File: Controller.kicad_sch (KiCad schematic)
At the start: 14 parts, among them SW1 PTS526 SK15 SMTR2 LFS, SW2 DS04-254-2-01BK-SMT, U1 STM32WB55RCVx, Y1 ECS-320-8-33-RWY-TR, Y2 ECS-.327-9-12R-TR

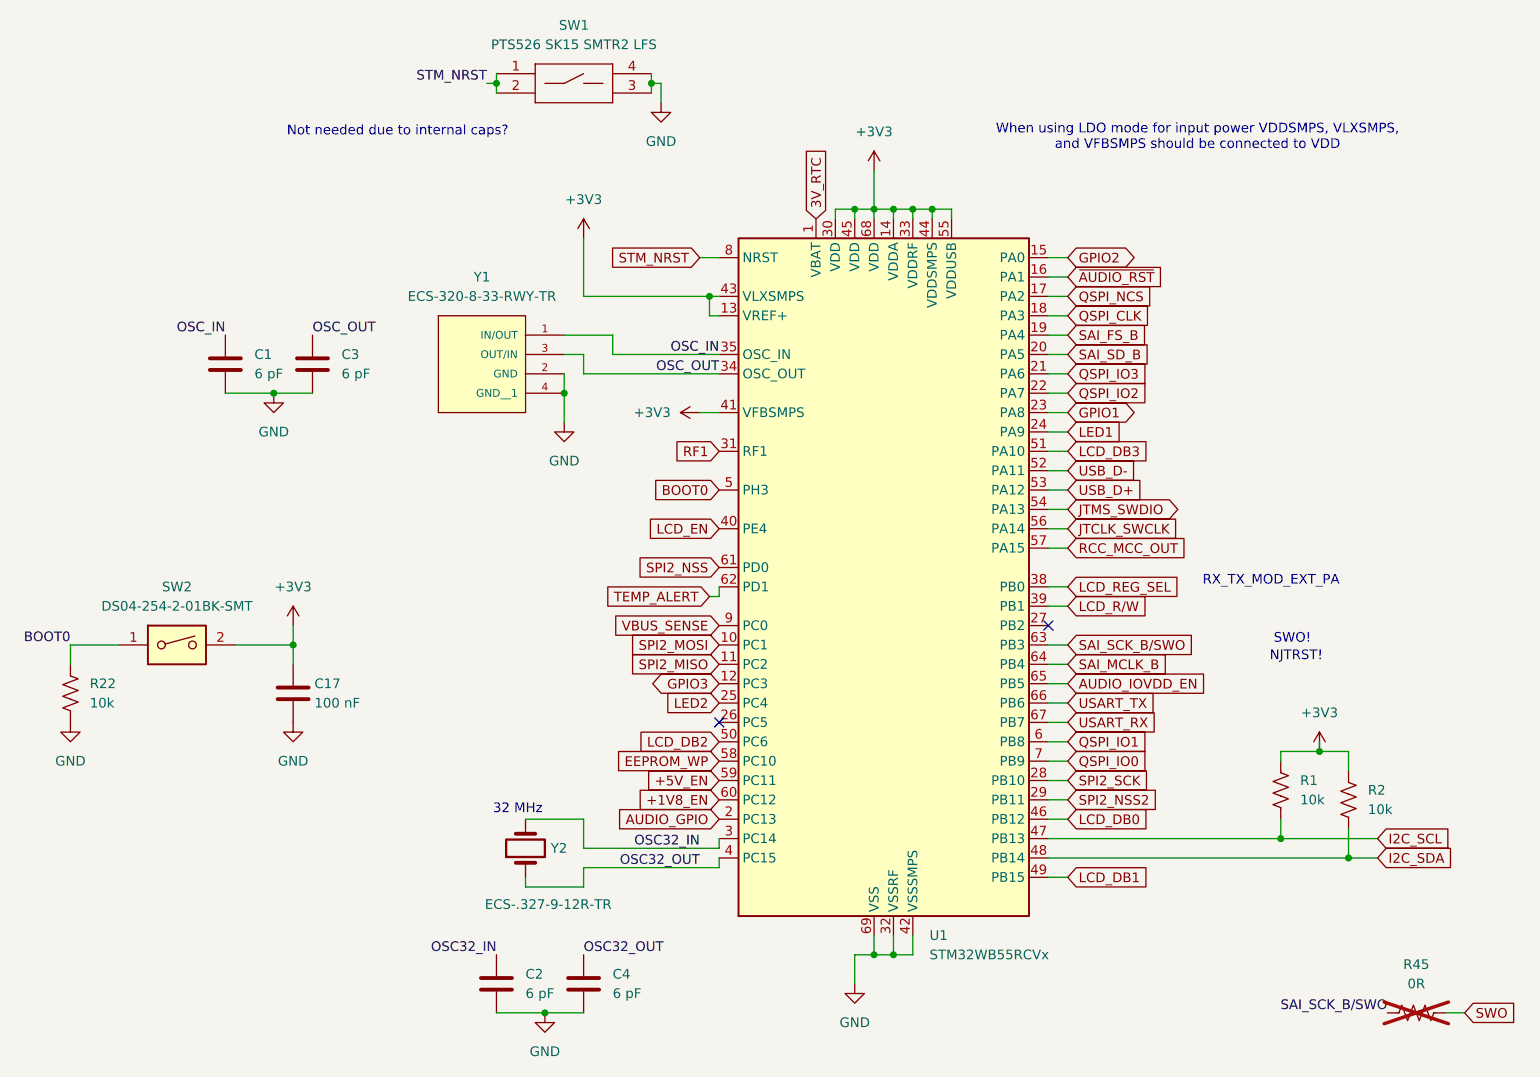
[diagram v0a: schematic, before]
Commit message: First draft of design output, schematic, and layout complete
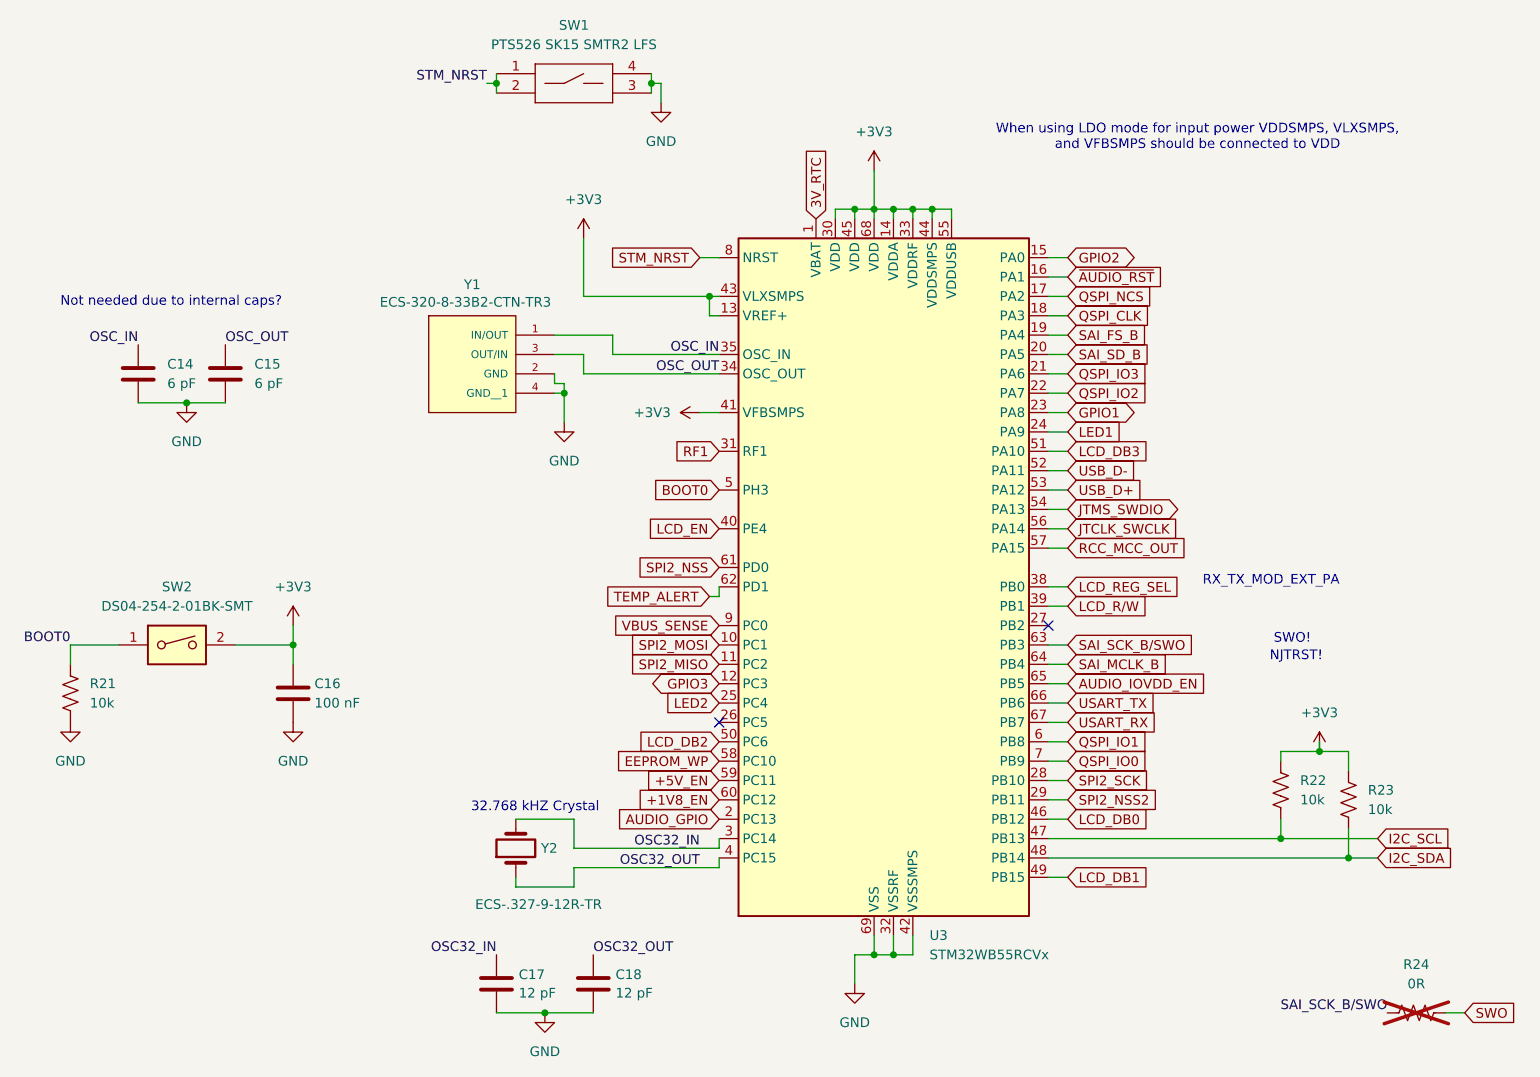
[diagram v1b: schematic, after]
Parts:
- C17: renamed from C2; value 6 pF -> 12 pF
- C18: renamed from C4; value 6 pF -> 12 pF
- Y1: value ECS-320-8-33-RWY-TR -> ECS-320-8-33B2-CTN-TR3
- renumbered C1 to C14, C3 to C15, C17 to C16, R22 to R21, R1 to R22, R2 to R23, R45 to R24, U1 to U3
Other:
- note added: "32.768 kHZ Crystal"
- note removed: "32 MHz"
- company: (none) -> Jacob Kapala
- moved on the sheet: C14, C15, C18, Y1, Y2
